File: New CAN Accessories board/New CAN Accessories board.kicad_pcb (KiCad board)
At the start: 2 copper layers, 106 x 91 mm, 99 parts, among them J1 39301040, J10 39301040, J11 ATF13-2P-BM03, J12 Conn_01x02_Pin, J2 39301040, J3 39301040, J4 39301040, J5 39301040, J6 39301040, J7 39301040, J8 39301040, J9 39301060, Q1 IRLML6344TRPBF, Q2 IRLML6344TRPBF, Q3 IRLML6344TRPBF, Q4 IRLML6344TRPBF, Q5 IRLML6344TRPBF, Q6 IRLML6344TRPBF, Q7 IRLML6344TRPBF, Q8 IRLML6344TRPBF, T1 MCP2562FD-E_SN, U1 NUCLEO_L432KC

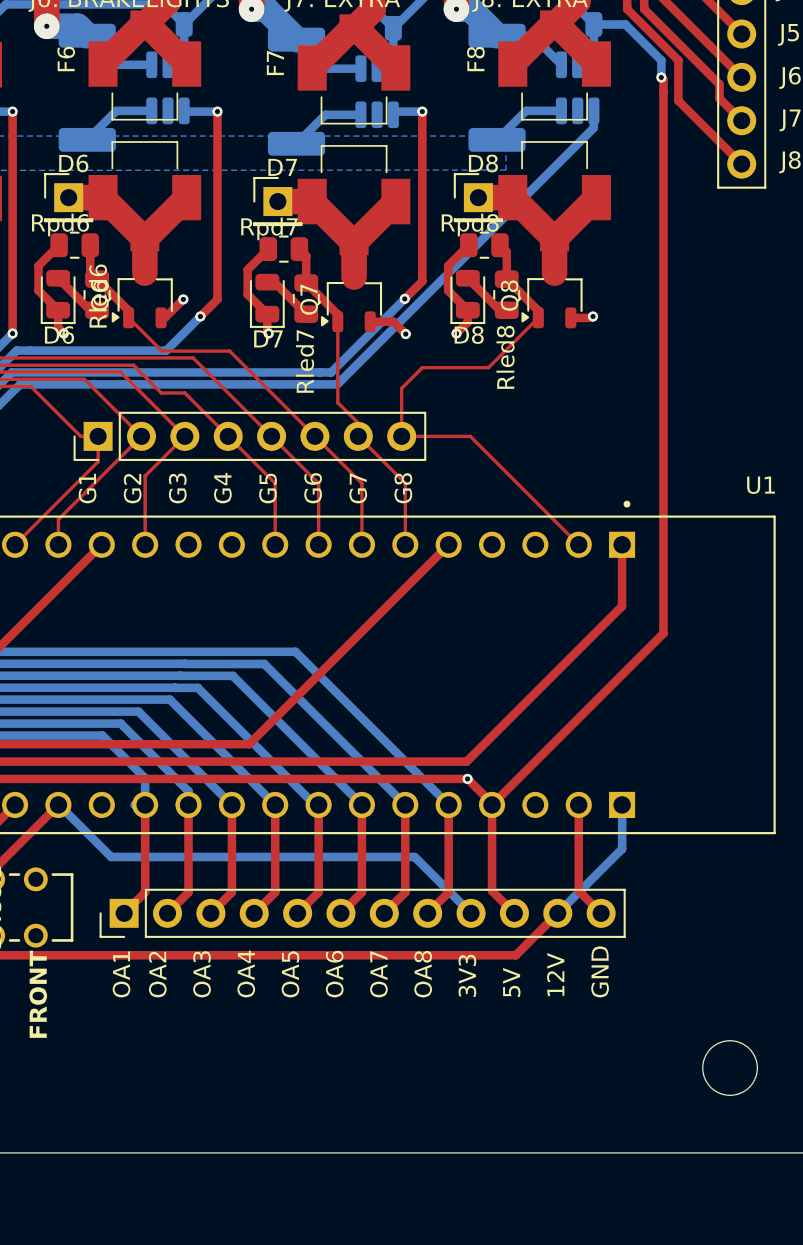
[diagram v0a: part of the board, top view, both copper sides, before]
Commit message: added supermileage logo and names
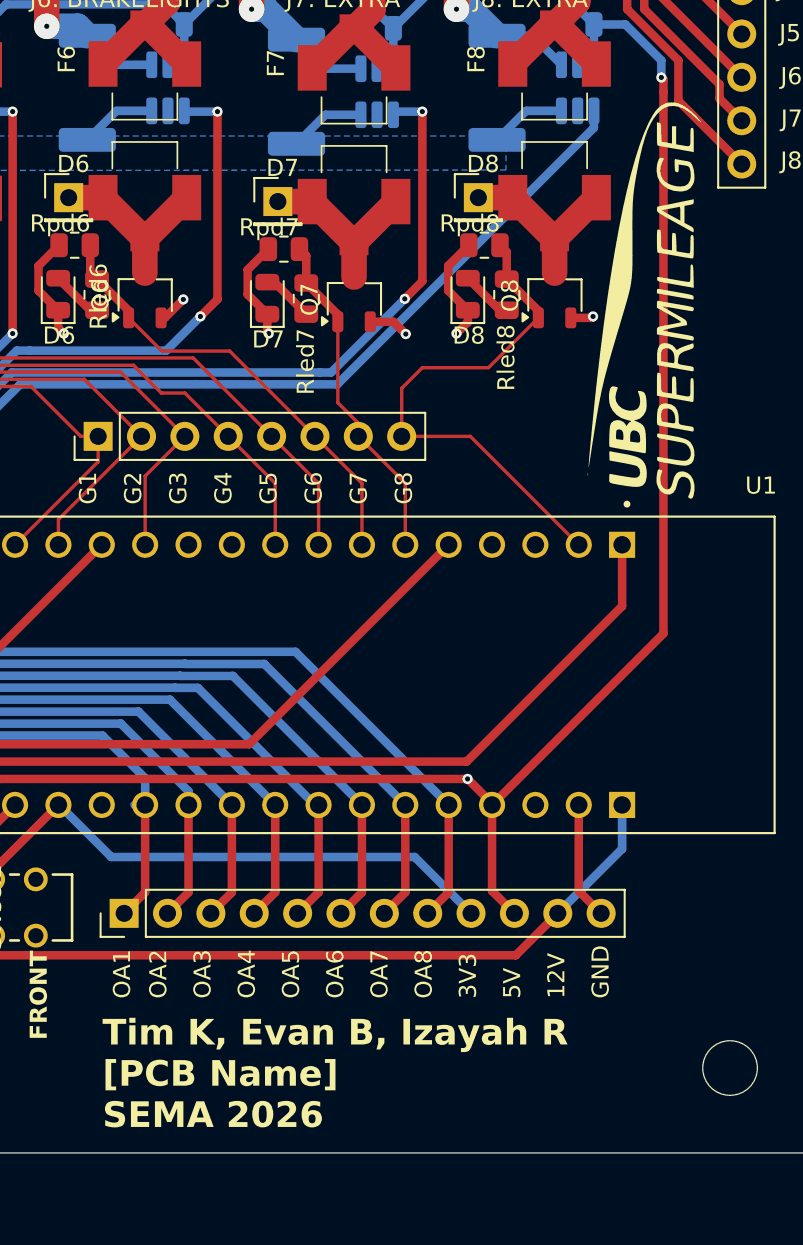
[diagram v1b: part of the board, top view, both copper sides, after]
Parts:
- added G***: LOGO, logo:logo, F.Cu at (112.1, 57.1)
- added G***: LOGO, logo:logo, B.Cu at (91.7, 79.2)
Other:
- board text added: "Tim K, Evan B, Izayah R [PCB Name] SEMA 2026"

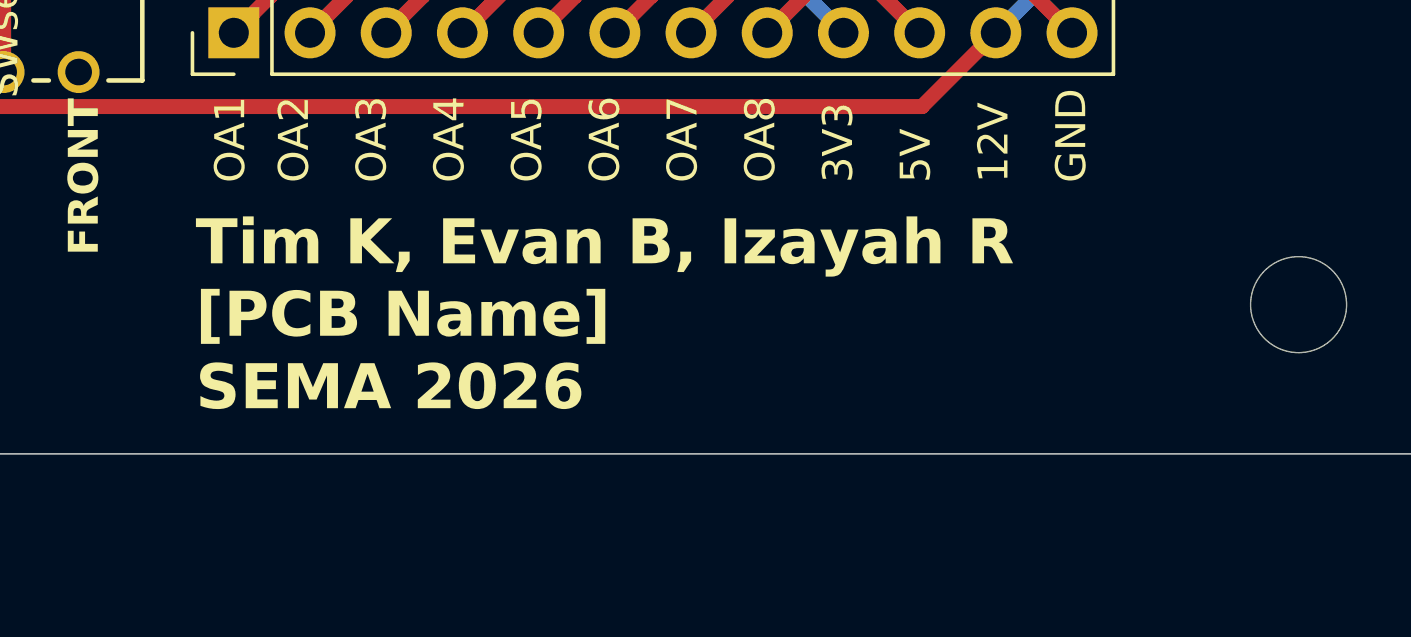
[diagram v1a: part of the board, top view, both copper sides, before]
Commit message: added TVS diode to schematic
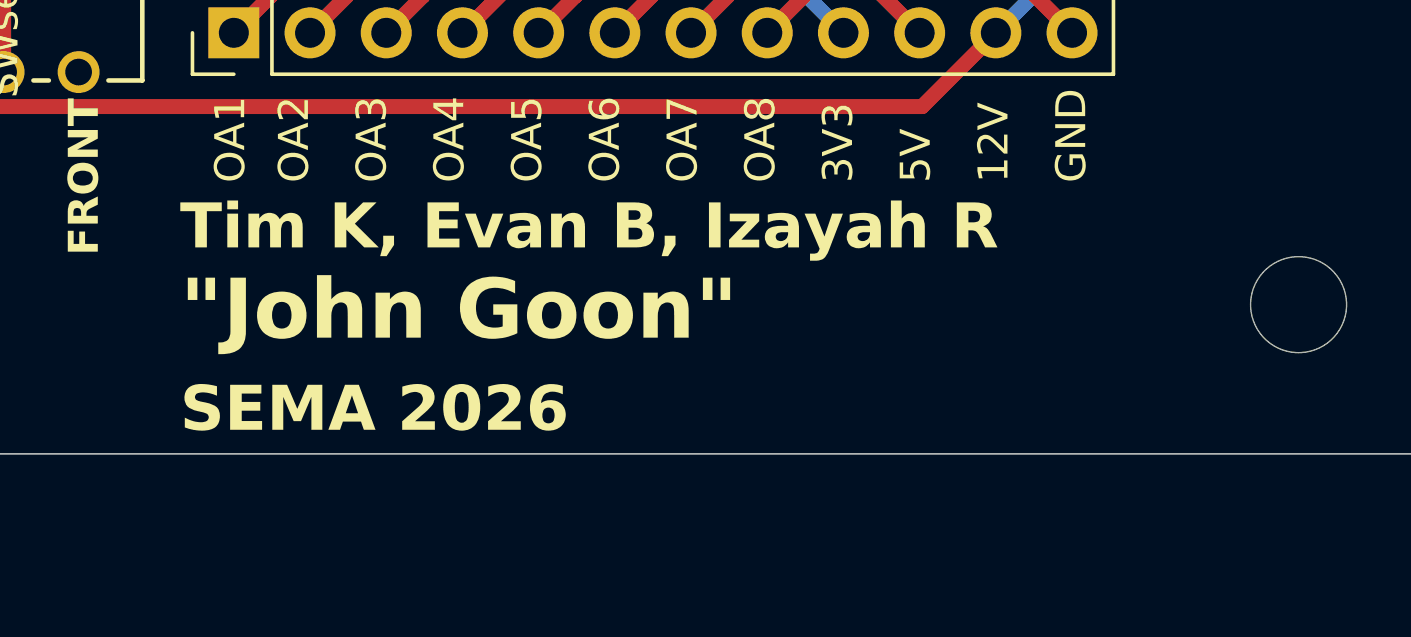
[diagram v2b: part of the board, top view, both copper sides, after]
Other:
- board text added: "SEMA 2026"
- board text added: "Tim K, Evan B, Izayah R"
- board text added: "{dblquote}John Goon{dblquote}"
- board text removed: "Tim K, Evan B, Izayah R [PCB Name] SEMA 2026"

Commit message: hmmm
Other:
- board text added: "{dblquote} John Goon {dblquote}"
- board text removed: "{dblquote}John Goon{dblquote}"

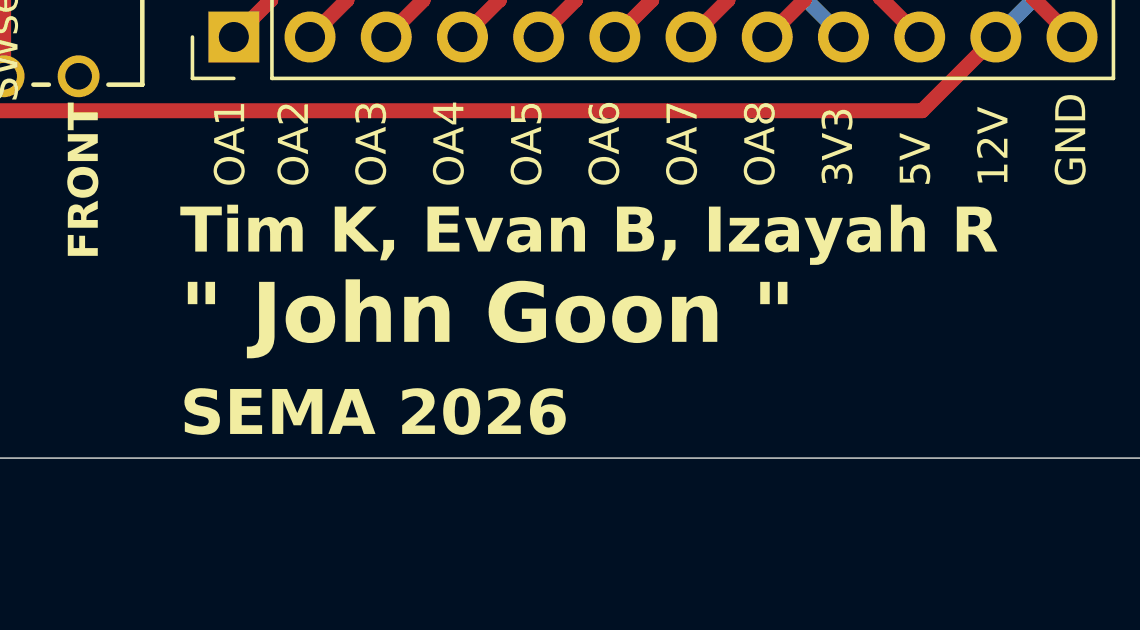
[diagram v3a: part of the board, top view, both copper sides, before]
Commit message: started making drain test point changes
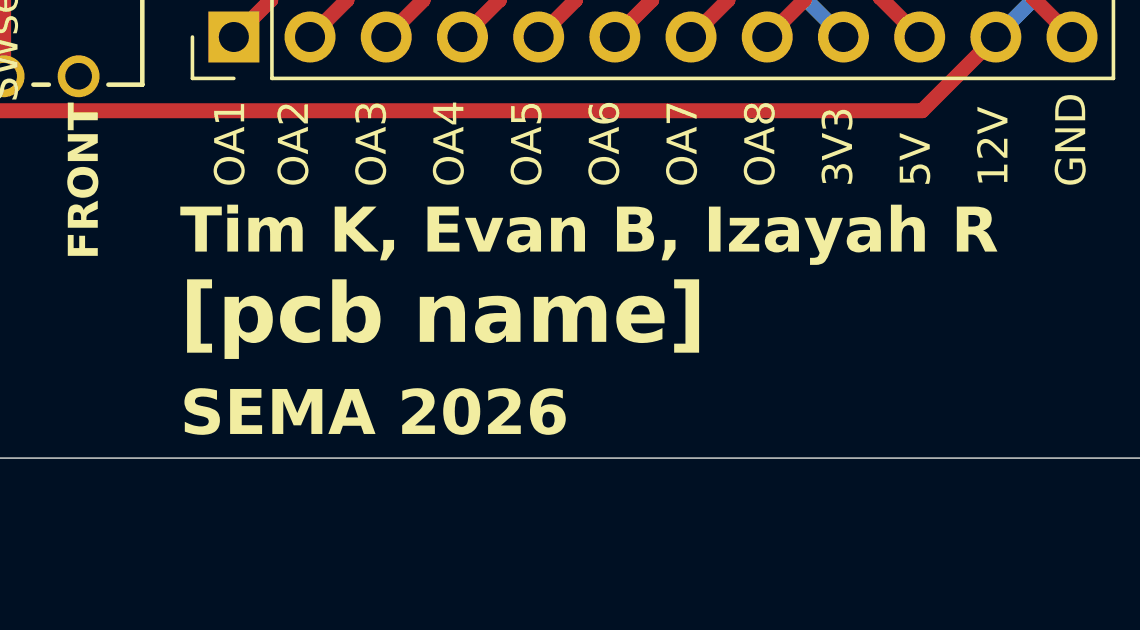
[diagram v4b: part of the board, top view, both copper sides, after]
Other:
- board text added: "[pcb name]"
- board text removed: "{dblquote} John Goon {dblquote}"

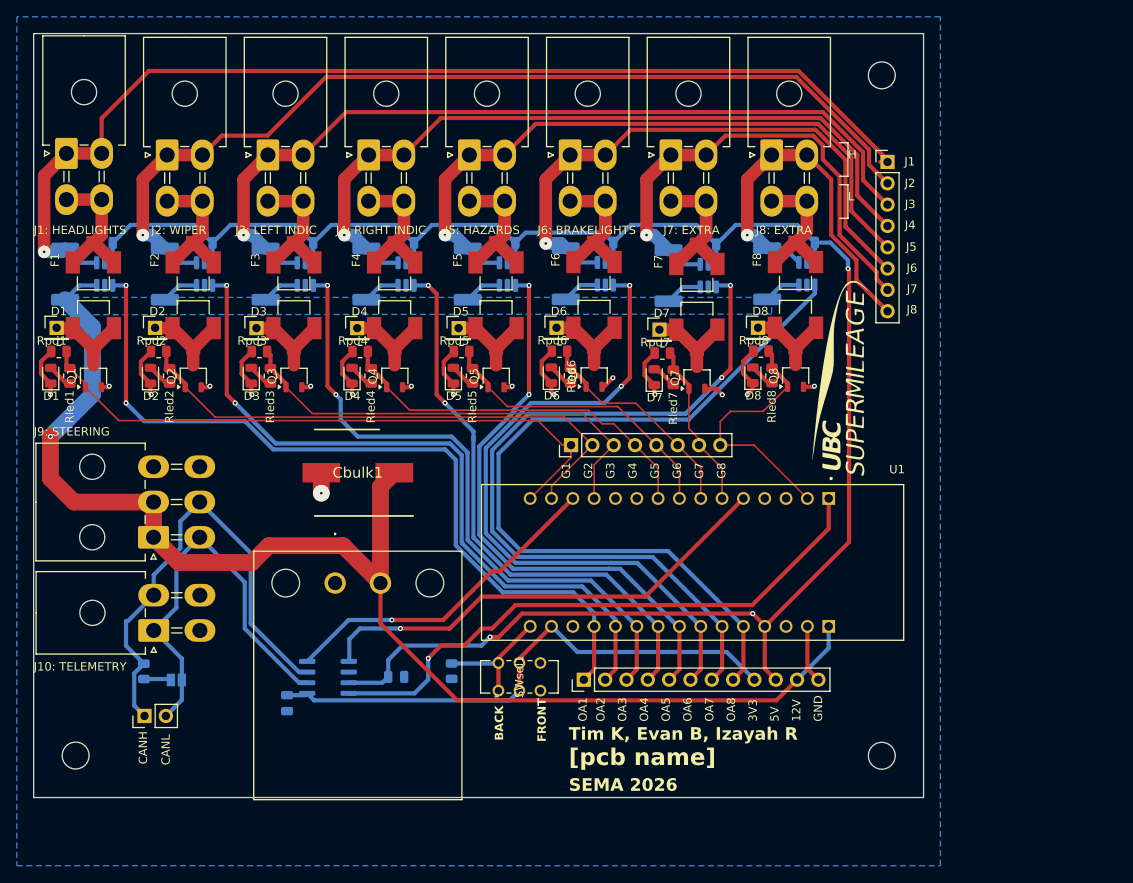
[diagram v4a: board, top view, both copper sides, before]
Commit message: 1x16 header test points
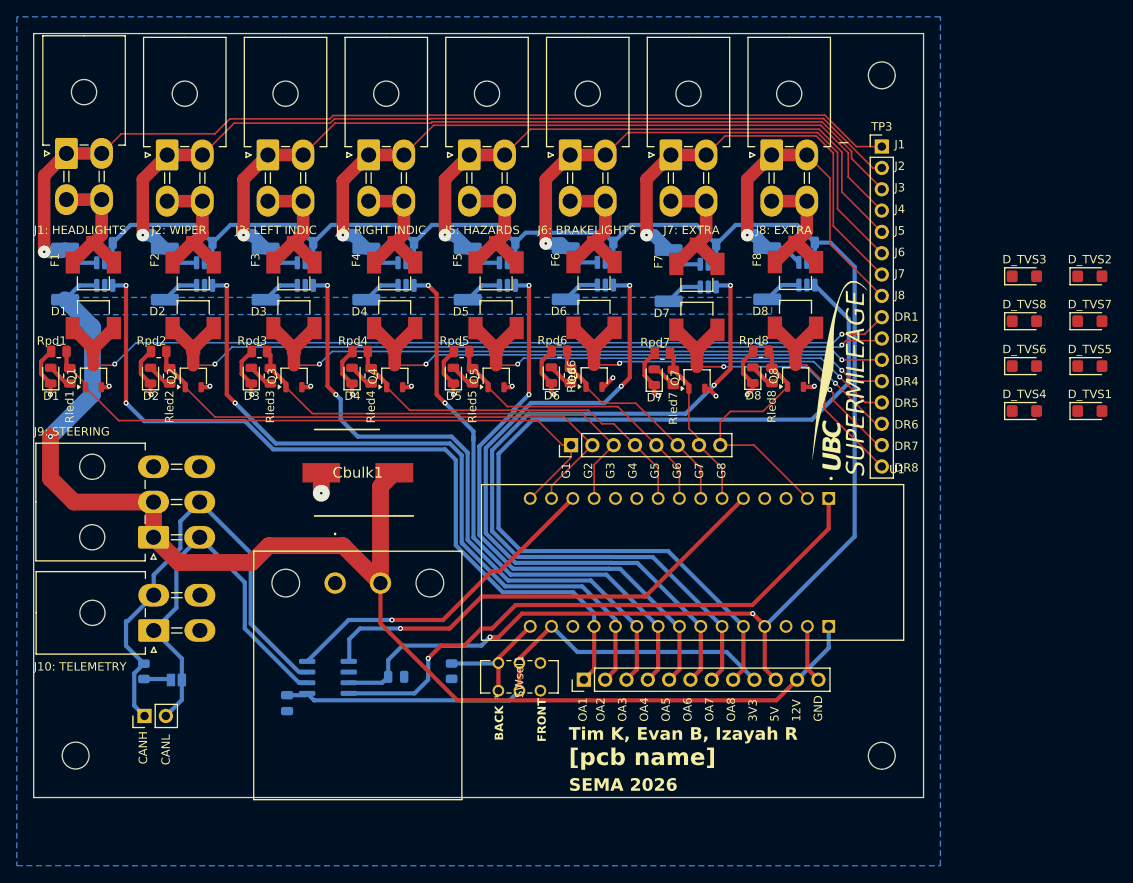
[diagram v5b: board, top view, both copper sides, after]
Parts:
- removed TP5: Conn_01x08_Pin, Connector_PinHeader_2.54mm:PinHeader_1x08_P2.54mm_Vertical
- removed TPdr1, TPdr2, TPdr3, TPdr4, TPdr5, TPdr6, TPdr7, TPdr8: TestPoint, Connector_PinHeader_2.54mm:PinHeader_1x01_P2.54mm_Vertical
- added D_TVS1: D_Zener, Diode_SMD:D_SMF, F.Cu at (141.8, 61.0)
- added D_TVS2: D_Zener, Diode_SMD:D_SMF, F.Cu at (141.8, 44.9)
- added D_TVS3: D_Zener, Diode_SMD:D_SMF, F.Cu at (134.0, 44.9)
- added D_TVS4: D_Zener, Diode_SMD:D_SMF, F.Cu at (134.0, 61.0)
- added D_TVS5: D_Zener, Diode_SMD:D_SMF, F.Cu at (141.8, 55.6)
- added D_TVS6: D_Zener, Diode_SMD:D_SMF, F.Cu at (134.0, 55.6)
- added D_TVS7: D_Zener, Diode_SMD:D_SMF, F.Cu at (141.8, 50.3)
- added D_TVS8: D_Zener, Diode_SMD:D_SMF, F.Cu at (134.0, 50.3)
- added TP3: Conn_01x16_Pin, Connector_PinHeader_2.54mm:PinHeader_1x16_P2.54mm_Vertical, F.Cu at (117.0, 29.5)
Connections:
- net Net-(F1-Pad2) renamed /TPdr1
- net Net-(F2-Pad2) renamed /TPdr2
- net Net-(F3-Pad2) renamed /TPdr3
- net Net-(F4-Pad2) renamed /TPdr4
- net Net-(F5-Pad2) renamed /TPdr5
- net Net-(F6-Pad2) renamed /TPdr6
- net Net-(F7-Pad2) renamed /TPdr7
- net Net-(F8-Pad2) renamed /TPdr8
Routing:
- net /TPdr1: track 10.9 -> 105.2 mm, vias 0 -> 2
- net /TPdr2: track 11.0 -> 92.3 mm, vias 0 -> 2
- net /TPdr3: track 10.9 -> 80.0 mm, vias 0 -> 2
- net /TPdr4: track 10.9 -> 68.8 mm, vias 0 -> 2
- net /TPdr5: track 10.9 -> 57.4 mm, vias 0 -> 2
- net /TPdr6: track 10.9 -> 46.4 mm, vias 0 -> 2
- net /TPdr7: track 10.9 -> 35.3 mm, vias 0 -> 2
- net /TPdr8: track 10.9 -> 26.0 mm
- net /OA8: track 96.3 -> 108.3 mm
- net /TPj1: track 129.8 -> 120.5 mm
- net /TPj2: track 114.5 -> 107.9 mm
- net /TPj3: track 100.9 -> 97.1 mm
- net /TPj4: track 90.3 -> 87.3 mm
- net /TPj5: track 79.8 -> 76.8 mm
- net /TPj6: track 69.4 -> 67.0 mm
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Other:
- board text removed: "H"
- board text removed: "J1"
- board text removed: "J2"
- board text removed: "J3"
- board text removed: "J4"
- board text removed: "J5"
- board text removed: "J6"
- board text removed: "J7"
- board text removed: "J8"
- board text removed: "L"

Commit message: TVS Diode added
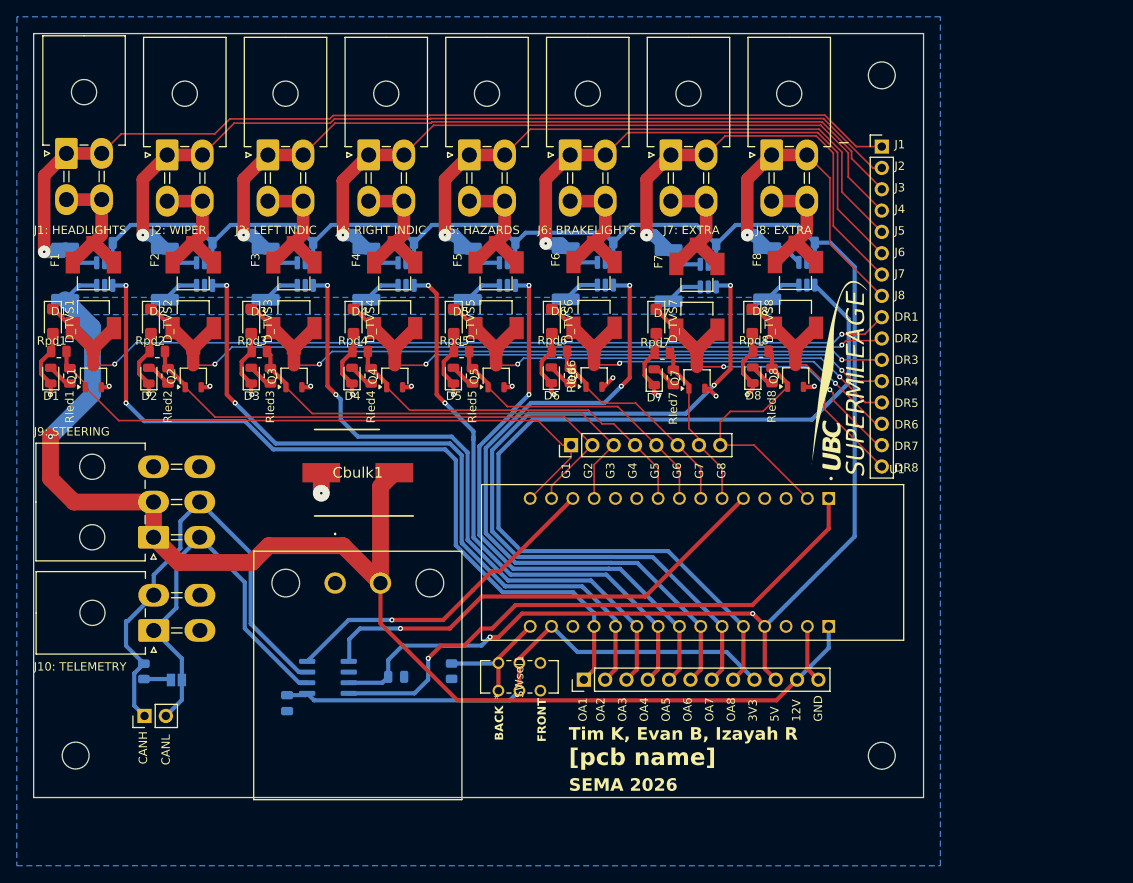
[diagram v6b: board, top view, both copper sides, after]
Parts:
- moved D_TVS1 124.0 mm to (18.3, 50.3), turned to -90 degrees
- moved D_TVS2 112.0 mm to (30.0, 50.3), turned to -90 degrees
- moved D_TVS3 92.3 mm to (41.9, 50.3), turned to -90 degrees
- moved D_TVS4 80.6 mm to (54.1, 50.3), turned to -90 degrees
- moved D_TVS5 76.0 mm to (66.0, 50.3), turned to -90 degrees
- moved D_TVS6 56.5 mm to (77.7, 50.3), turned to -90 degrees
- moved D_TVS7 51.6 mm to (90.2, 50.3), turned to -90 degrees
- moved D_TVS8 32.4 mm to (101.6, 50.3), turned to -90 degrees
- moved D2 0.20 mm to (29.7, 56.7)
- moved Rled2 0.20 mm to (32.0, 56.8)
- moved Rpd2 0.16 mm to (30.7, 53.9)
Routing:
- net GND: track 69.0 -> 86.8 mm
- net /TPdr2: track 92.3 -> 96.1 mm
- net /TPdr8: track 26.0 -> 29.7 mm
- net /TPdr3: track 80.0 -> 83.6 mm
- net /TPdr5: track 57.4 -> 60.9 mm
- net /TPdr6: track 46.4 -> 49.9 mm
- net /TPdr7: track 35.3 -> 38.8 mm
- net /TPdr1: track 105.2 -> 108.7 mm
- net /TPdr4: track 68.8 -> 72.2 mm
